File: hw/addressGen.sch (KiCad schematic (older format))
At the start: 8 parts, among them U101 74LS08, U102 74LS08, U103 74LS283, U104 74LS283, U105 74LS283, U106 74LS283, U107 74LS574, U108 74LS574

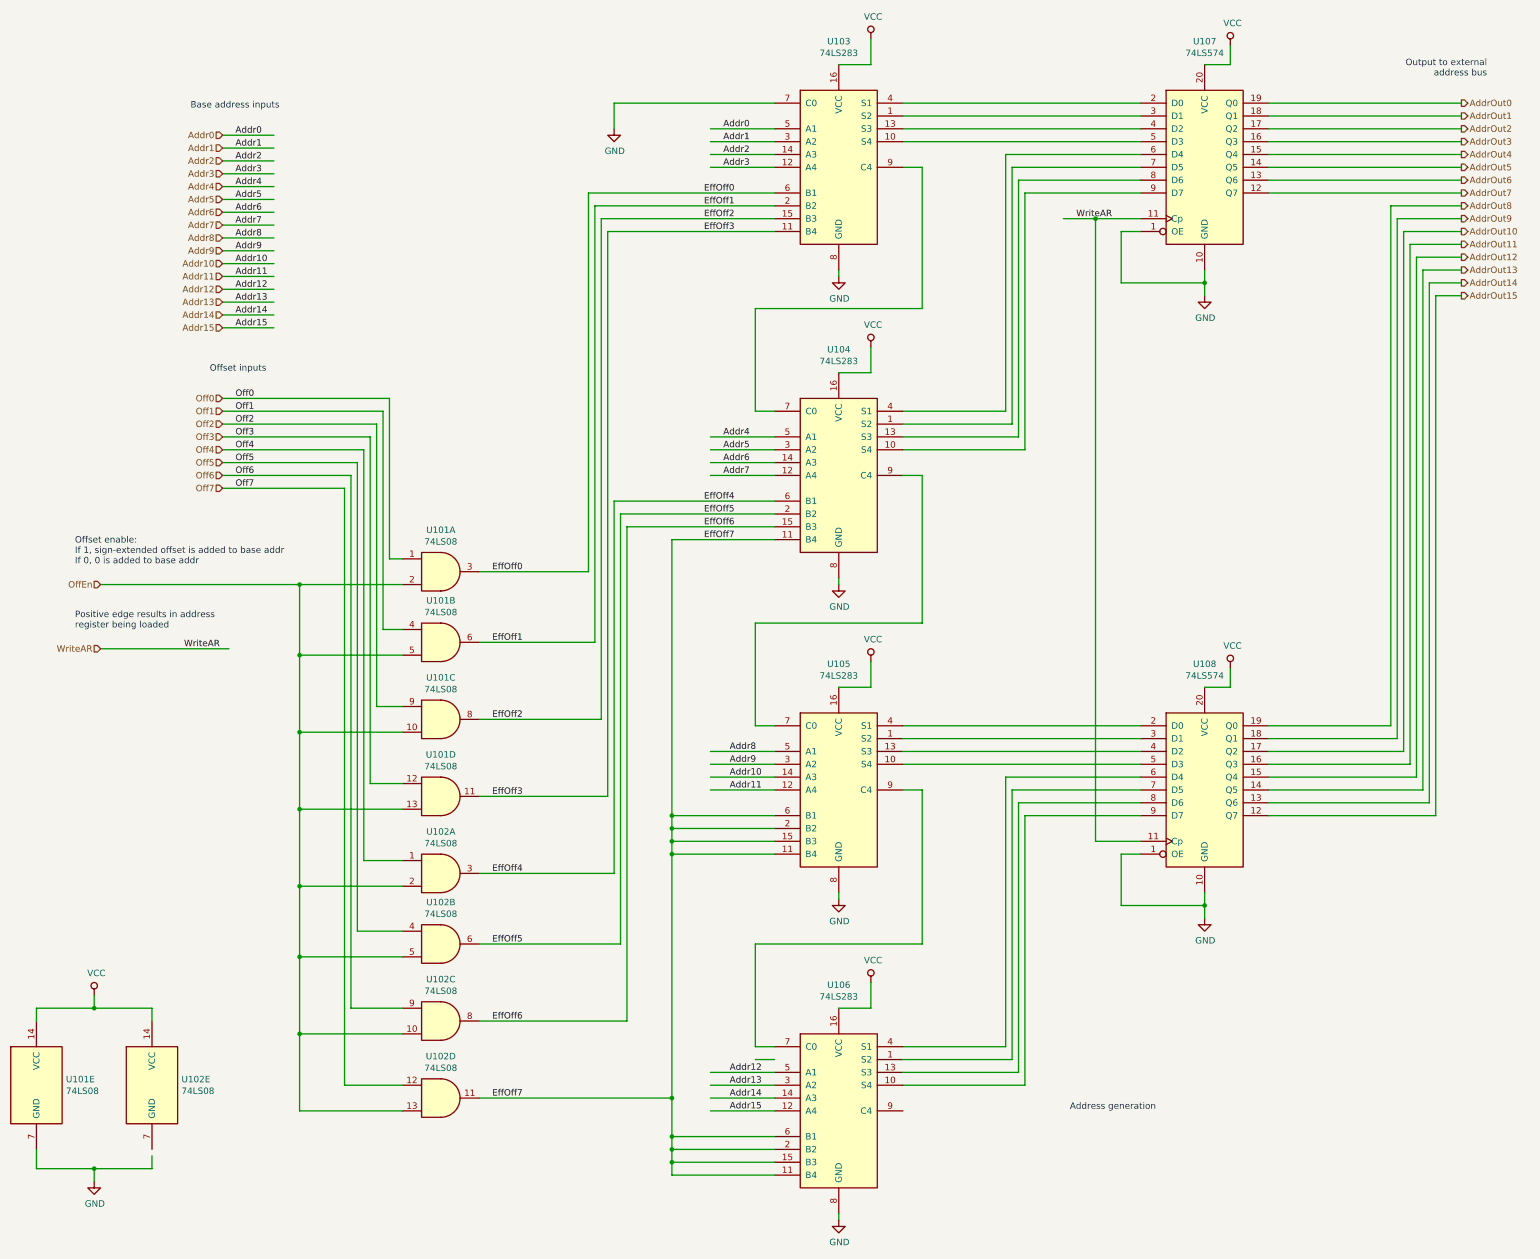
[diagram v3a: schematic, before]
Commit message: program counter is now 2x 74HCT574
Increment is done using the address generation unit,
and the output of address generation can be optionally
sent back to the address registers (such as PC)
via buffers.

This hugely simplifies the program counter implementation,
and also makes it easy to provide additional address
registers (X, SP) that can benefit from increment
and decrement operations.
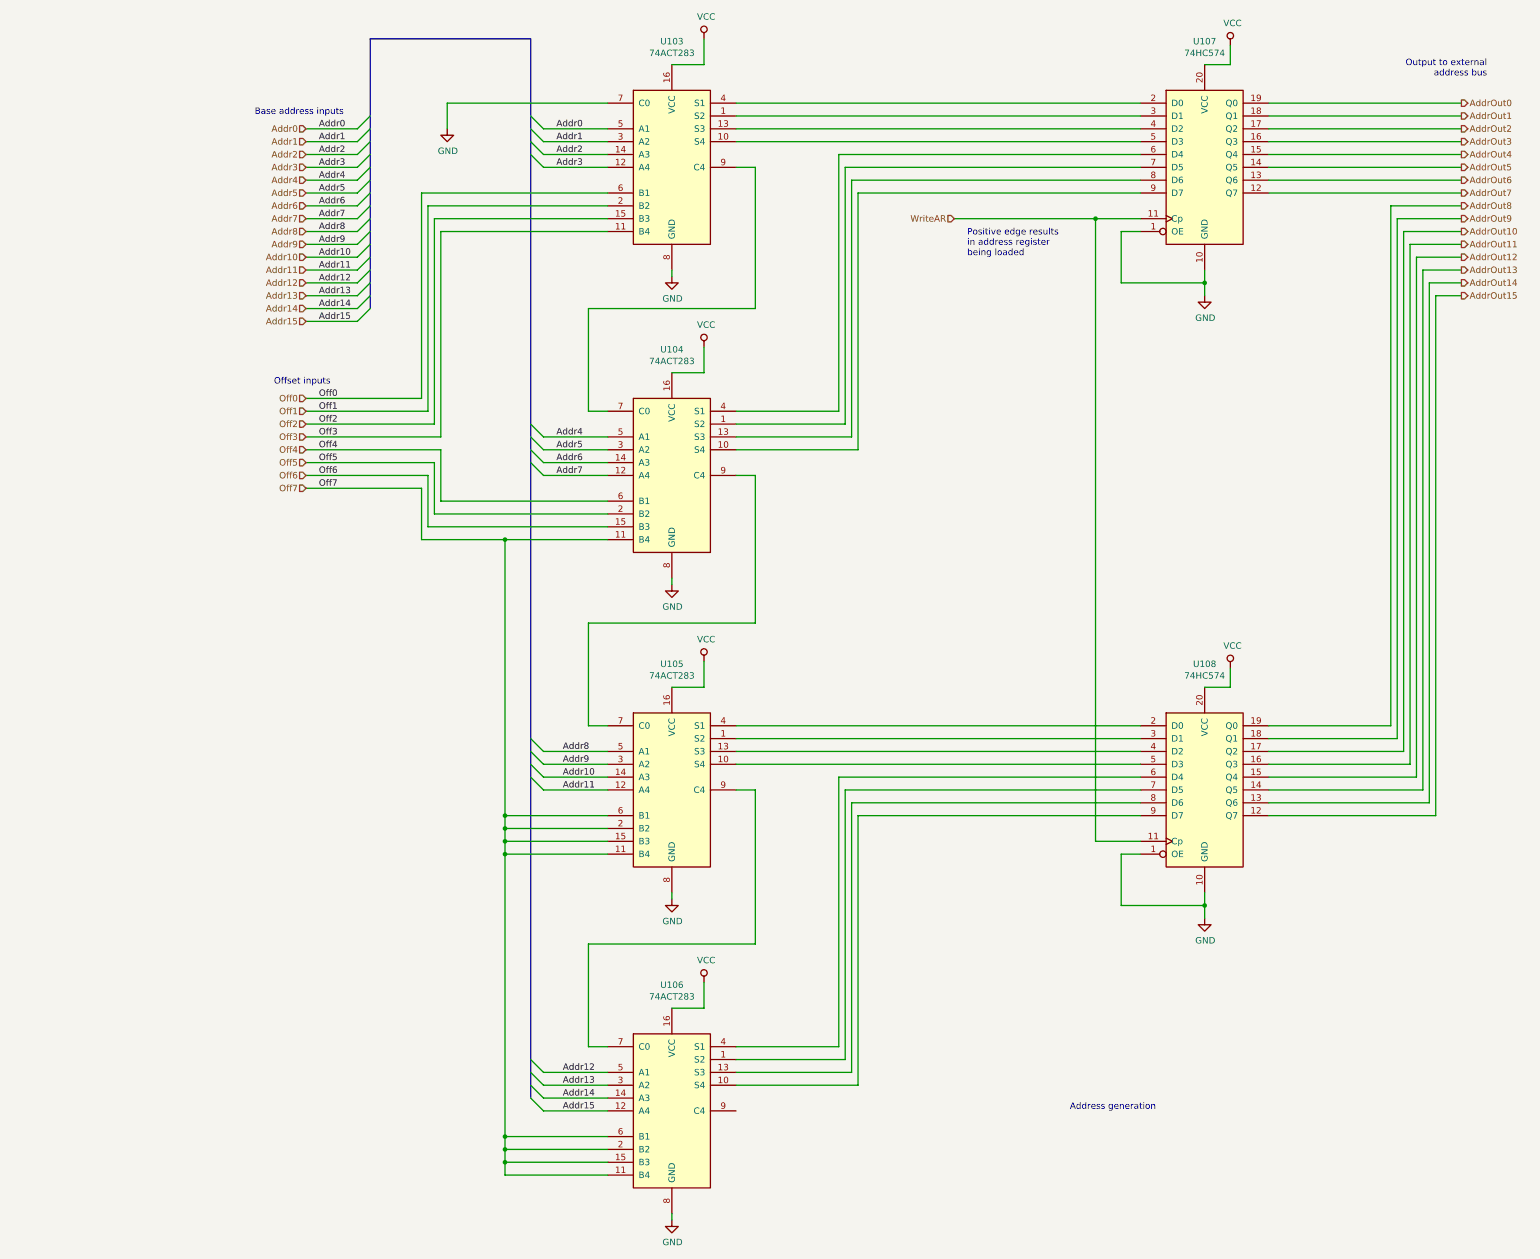
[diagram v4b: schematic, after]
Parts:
- removed U101, U102: 74LS08, symbol 74xx:74LS08
- U103, U104, U105, U106: value 74LS283 -> 74ACT283
- U107, U108: value 74LS574 -> 74HC574
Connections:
- net labels removed: EffOff0, EffOff1, EffOff2, EffOff3, EffOff4, EffOff5, EffOff6, EffOff7, OffEn
- wire segments 235 -> 184
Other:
- note added: "Positive edge results\nin address register\nbeing loaded"
- note removed: "Offset enable:\nIf 1, sign-extended offset is added to base addr\nIf 0, 0 is added to base addr"
- note removed: "Positive edge results in address\nregister being loaded"
- moved on the sheet: U103, U104, U105, U106
